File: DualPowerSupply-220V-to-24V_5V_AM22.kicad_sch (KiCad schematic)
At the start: 7 parts, among them U1 AM22-24W2405V

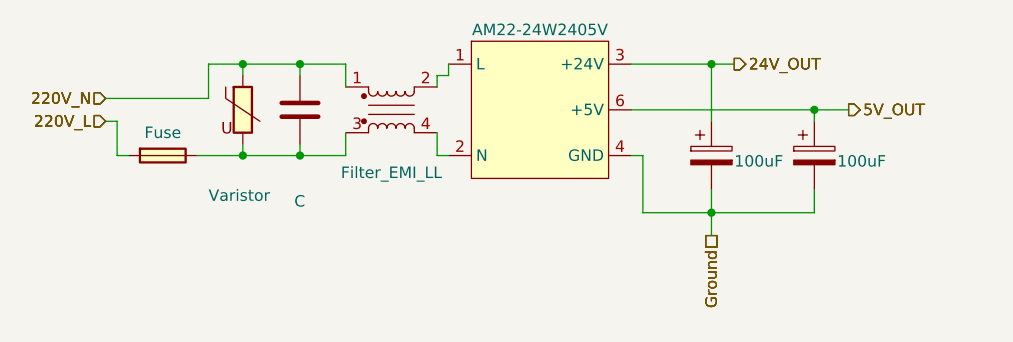
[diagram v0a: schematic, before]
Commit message: finish some unconnect pins, draw edge cut board
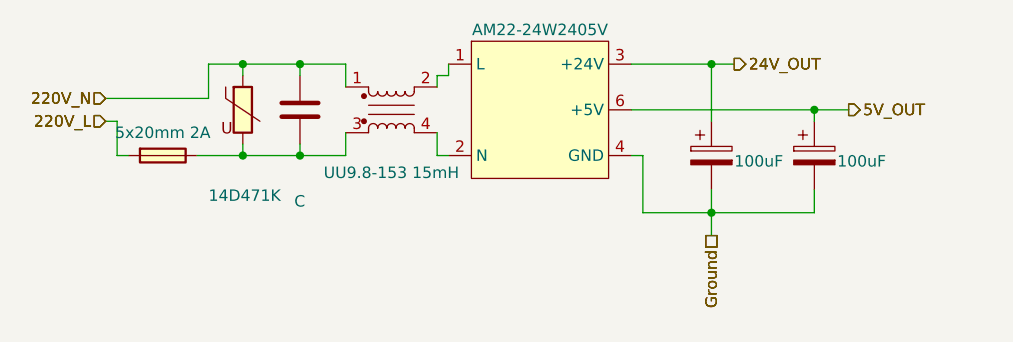
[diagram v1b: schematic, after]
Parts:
- F1: value Fuse -> 5x20mm 2A
- FL1: value Filter_EMI_LL -> UU9.8-153 15mH
- RV1: value Varistor -> 14D471K
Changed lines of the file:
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@@
 			)
 		)
-		(property "Value" "Fuse"
+		(property "Value" "5x20mm 2A"
 			(at 96.52 99.06 0)
 			(effects
@@
 			)
 		)
-		(property "Value" "Filter_EMI_LL"
+		(property "Value" "UU9.8-153 15mH"
 			(at 121.92 103.505 0)
 			(effects
@@
 			)
 		)
-		(property "Value" "Varistor"
+		(property "Value" "14D471K"
 			(at 101.6 106.045 0)
 			(effects

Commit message: layout p1
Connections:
- net 220V_N: now also FL1.3; no longer FL1.1
- net at C1.2, F1.2, RV1.2: now also FL1.1; no longer FL1.3
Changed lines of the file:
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@@
 	)
 	(junction
-		(at 157.48 107.95)
+		(at 163.83 107.95)
 		(diameter 0)
 		(color 0 0 0 0)
@@
 	)
 	(junction
-		(at 157.48 91.44)
+		(at 163.83 91.44)
 		(diameter 0)
 		(color 0 0 0 0)
 	)
 	(junction
-		(at 168.91 96.52)
+		(at 175.26 96.52)
 		(diameter 0)
 		(color 0 0 0 0)
@@
 	(wire
 		(pts
-			(xy 127 92.71) (xy 127 93.98)
-		)
-		(stroke
-			(width 0)
-			(type default)
-		)
-	)
-	(wire
-		(pts
-			(xy 148.59 96.52) (xy 168.91 96.52)
+			(xy 154.94 96.52) (xy 175.26 96.52)
 		)
 		(stroke
@@
 	(wire
 		(pts
-			(xy 149.86 107.95) (xy 149.86 101.6)
+			(xy 156.21 107.95) (xy 156.21 101.6)
 		)
 		(stroke
@@
 	(wire
 		(pts
-			(xy 127 92.71) (xy 128.27 92.71)
-		)
-		(stroke
-			(width 0)
-			(type default)
-		)
-	)
-	(wire
-		(pts
-			(xy 160.02 91.44) (xy 157.48 91.44)
-		)
-		(stroke
-			(width 0)
-			(type default)
-		)
-	)
-	(wire
-		(pts
-			(xy 127 99.06) (xy 127 101.6)
-		)
-		(stroke
-			(width 0)
-			(type default)
-		)
-	)
-	(wire
-		(pts
-			(xy 127 101.6) (xy 128.27 101.6)
-		)
-		(stroke
-			(width 0)
-			(type default)
-		)
-	)
-	(wire
-		(pts
-			(xy 128.27 92.71) (xy 128.27 91.44)
+			(xy 166.37 91.44) (xy 163.83 91.44)
+		)
+		(stroke
+			(width 0)
+			(type default)
+		)
+	)
+	(wire
+		(pts
+			(xy 130.81 93.98) (xy 130.81 101.6)
+		)
+		(stroke
+			(width 0)
+			(type default)
+		)
+	)
+	(wire
+		(pts
+			(xy 127 99.06) (xy 134.62 99.06)
 		)
 		(stroke
@@
 	(wire
 		(pts
+			(xy 127 93.98) (xy 130.81 93.98)
+		)
+		(stroke
+			(width 0)
+			(type default)
+		)
+	)
+	(wire
+		(pts
 			(xy 111.76 100.33) (xy 111.76 101.6)
 		)
@@
 	(wire
 		(pts
-			(xy 157.48 91.44) (xy 157.48 97.79)
-		)
-		(stroke
-			(width 0)
-			(type default)
-		)
-	)
-	(wire
-		(pts
-			(xy 168.91 96.52) (xy 168.91 97.79)
+			(xy 163.83 91.44) (xy 163.83 97.79)
+		)
+		(stroke
+			(width 0)
+			(type default)
+		)
+	)
+	(wire
+		(pts
+			(xy 175.26 96.52) (xy 175.26 97.79)
 		)
 		(stroke
@@
 	(wire
 		(pts
-			(xy 157.48 105.41) (xy 157.48 107.95)
-		)
-		(stroke
-			(width 0)
-			(type default)
-		)
-	)
-	(wire
-		(pts
-			(xy 168.91 105.41) (xy 168.91 107.95)
-		)
-		(stroke
-			(width 0)
-			(type default)
-		)
-	)
-	(wire
-		(pts
-			(xy 148.59 91.44) (xy 157.48 91.44)
+			(xy 163.83 105.41) (xy 163.83 107.95)
+		)
+		(stroke
+			(width 0)
+			(type default)
+		)
+	)
+	(wire
+		(pts
+			(xy 175.26 105.41) (xy 175.26 107.95)
+		)
+		(stroke
+			(width 0)
+			(type default)
+		)
+	)
+	(wire
+		(pts
+			(xy 154.94 91.44) (xy 163.83 91.44)
 		)
 		(stroke
@@
 	(wire
 		(pts
-			(xy 157.48 107.95) (xy 157.48 110.49)
+			(xy 163.83 107.95) (xy 163.83 110.49)
+		)
+		(stroke
+			(width 0)
+			(type default)
+		)
+	)
+	(wire
+		(pts
+			(xy 134.62 99.06) (xy 134.62 91.44)
 		)
 		(stroke
@@
 	(wire
 		(pts
-			(xy 168.91 96.52) (xy 172.72 96.52)
-		)
-		(stroke
-			(width 0)
-			(type default)
-		)
-	)
-	(wire
-		(pts
-			(xy 149.86 101.6) (xy 148.59 101.6)
-		)
-		(stroke
-			(width 0)
-			(type default)
-		)
-	)
-	(wire
-		(pts
-			(xy 168.91 107.95) (xy 157.48 107.95)
+			(xy 130.81 101.6) (xy 134.62 101.6)
+		)
+		(stroke
+			(width 0)
+			(type default)
+		)
+	)
+	(wire
+		(pts
+			(xy 175.26 96.52) (xy 179.07 96.52)
+		)
+		(stroke
+			(width 0)
+			(type default)
+		)
+	)
+	(wire
+		(pts
+			(xy 156.21 101.6) (xy 154.94 101.6)
+		)
+		(stroke
+			(width 0)
+			(type default)
+		)
+	)
+	(wire
+		(pts
+			(xy 175.26 107.95) (xy 163.83 107.95)
 		)
 		(stroke
@@
 	(wire
 		(pts
-			(xy 149.86 107.95) (xy 157.48 107.95)
+			(xy 156.21 107.95) (xy 163.83 107.95)
 		)
 		(stroke
@@
 	(hierarchical_label "24V_OUT"
 		(shape output)
-		(at 160.02 91.44 0)
+		(at 166.37 91.44 0)
 		(fields_autoplaced yes)
 		(effects
@@
 	(hierarchical_label "24V_OUT"
 		(shape output)
-		(at 160.02 91.44 0)
+		(at 166.37 91.44 0)
 		(fields_autoplaced yes)
 		(effects
@@
 	(hierarchical_label "Ground"
 		(shape passive)
-		(at 157.48 110.49 270)
+		(at 163.83 110.49 270)
 		(fields_autoplaced yes)
 		(effects
@@
 	(hierarchical_label "Ground"
 		(shape passive)
-		(at 157.48 110.49 270)
+		(at 163.83 110.49 270)
 		(fields_autoplaced yes)
 		(effects
@@
 	(hierarchical_label "5V_OUT"
 		(shape output)
-		(at 172.72 96.52 0)
+		(at 179.07 96.52 0)
 		(fields_autoplaced yes)
 		(effects
@@
 	(hierarchical_label "5V_OUT"
 		(shape output)
-		(at 172.72 96.52 0)
+		(at 179.07 96.52 0)
 		(fields_autoplaced yes)
 		(effects
@@
 		(lib_id "IVS_SYMBOLS:Filter_EMI_LL")
 		(at 121.92 96.52 0)
+		(mirror x)
 		(unit 1)
 		(exclude_from_sim no)
@@
 		(dnp no)
 		(property "Reference" "FL1"
-			(at 121.92 100.965 0)
+			(at 121.92 92.075 0)
 			(effects
 				(font
@@
 		)
 		(property "Value" "UU9.8-153 15mH"
-			(at 121.92 103.505 0)
+			(at 121.92 89.535 0)
 			(effects
 				(font
@@
 		)
 		(property "Footprint" "SpiritBoi_Footprint_Library:ACFilterChoke-UU9.8"
-			(at 121.92 104.14 0)
+			(at 121.92 88.9 0)
 			(effects
 				(font
@@
 		)
 		(property "Datasheet" "~"
-			(at 121.92 95.504 0)
+			(at 121.92 97.536 0)
 			(effects
 				(font
@@
 	(symbol
 		(lib_id "Device:C_Polarized")
-		(at 168.91 101.6 0)
+		(at 175.26 101.6 0)
 		(unit 1)
 		(exclude_from_sim no)
@@
 		(dnp no)
 		(property "Reference" "C3"
-			(at 172.085 100.076 0)
+			(at 178.435 100.076 0)
 			(effects
 				(font
@@
 		)
 		(property "Value" "100uF"
-			(at 171.45 102.235 0)
+			(at 177.8 102.235 0)
 			(effects
 				(font
@@
 		)
 		(property "Footprint" "SpiritBoi_Footprint_Library:CP-Alu-SMD-8x10.5mm"
-			(at 169.8752 105.41 0)
+			(at 176.2252 105.41 0)
 			(effects
 				(font
@@
 		)
 		(property "Datasheet" "~"
-			(at 168.91 101.6 0)
+			(at 175.26 101.6 0)
 			(effects
 				(font
@@
 		)
 		(property "Description" ""
-			(at 168.91 101.6 0)
+			(at 175.26 101.6 0)
 			(effects
 				(font
@@
 	(symbol
 		(lib_id "SpiritBoi_Library:AM22-24W2405V")
-		(at 138.43 96.52 0)
+		(at 144.78 96.52 0)
 		(unit 1)
 		(exclude_from_sim no)
@@
 		(fields_autoplaced yes)
 		(property "Reference" "U1"
-			(at 138.43 85.09 0)
+			(at 144.78 85.09 0)
 			(effects
 				(font
@@
 		)
 		(property "Value" "AM22-24W2405V"
-			(at 138.43 87.63 0)
+			(at 144.78 87.63 0)
 			(effects
 				(font
@@
 		)
 		(property "Footprint" "SpiritBoi_Footprint_Library:DualPowerSupply-24W_24V_05V_AM22"
-			(at 138.43 96.52 0)
+			(at 144.78 96.52 0)
 			(effects
 				(font
@@
 		)
 		(property "Datasheet" ""
-			(at 138.43 96.52 0)
+			(at 144.78 96.52 0)
 			(effects
 				(font
@@
 		)
 		(property "Description" ""
-			(at 138.43 96.52 0)
+			(at 144.78 96.52 0)
 			(effects
 				(font
@@
 	(symbol
 		(lib_id "Device:C_Polarized")
-		(at 157.48 101.6 0)
+		(at 163.83 101.6 0)
 		(unit 1)
 		(exclude_from_sim no)
@@
 		(dnp no)
 		(property "Reference" "C2"
-			(at 160.655 100.076 0)
+			(at 167.005 100.076 0)
 			(effects
 				(font
@@
 		)
 		(property "Value" "100uF"
-			(at 160.02 102.235 0)
+			(at 166.37 102.235 0)
 			(effects
 				(font
@@
 		)
 		(property "Footprint" "SpiritBoi_Footprint_Library:CP-Alu-SMD-8x10.5mm"
-			(at 158.4452 105.41 0)
+			(at 164.7952 105.41 0)
 			(effects
 				(font
@@
 		)
 		(property "Datasheet" "~"
-			(at 157.48 101.6 0)
+			(at 163.83 101.6 0)
 			(effects
 				(font
@@
 		)
 		(property "Description" ""
-			(at 157.48 101.6 0)
-			(effects
-				(font
+			(at 163.83 101.6 0)
+			(effects
+				(font
